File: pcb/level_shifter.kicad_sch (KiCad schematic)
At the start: 9 parts

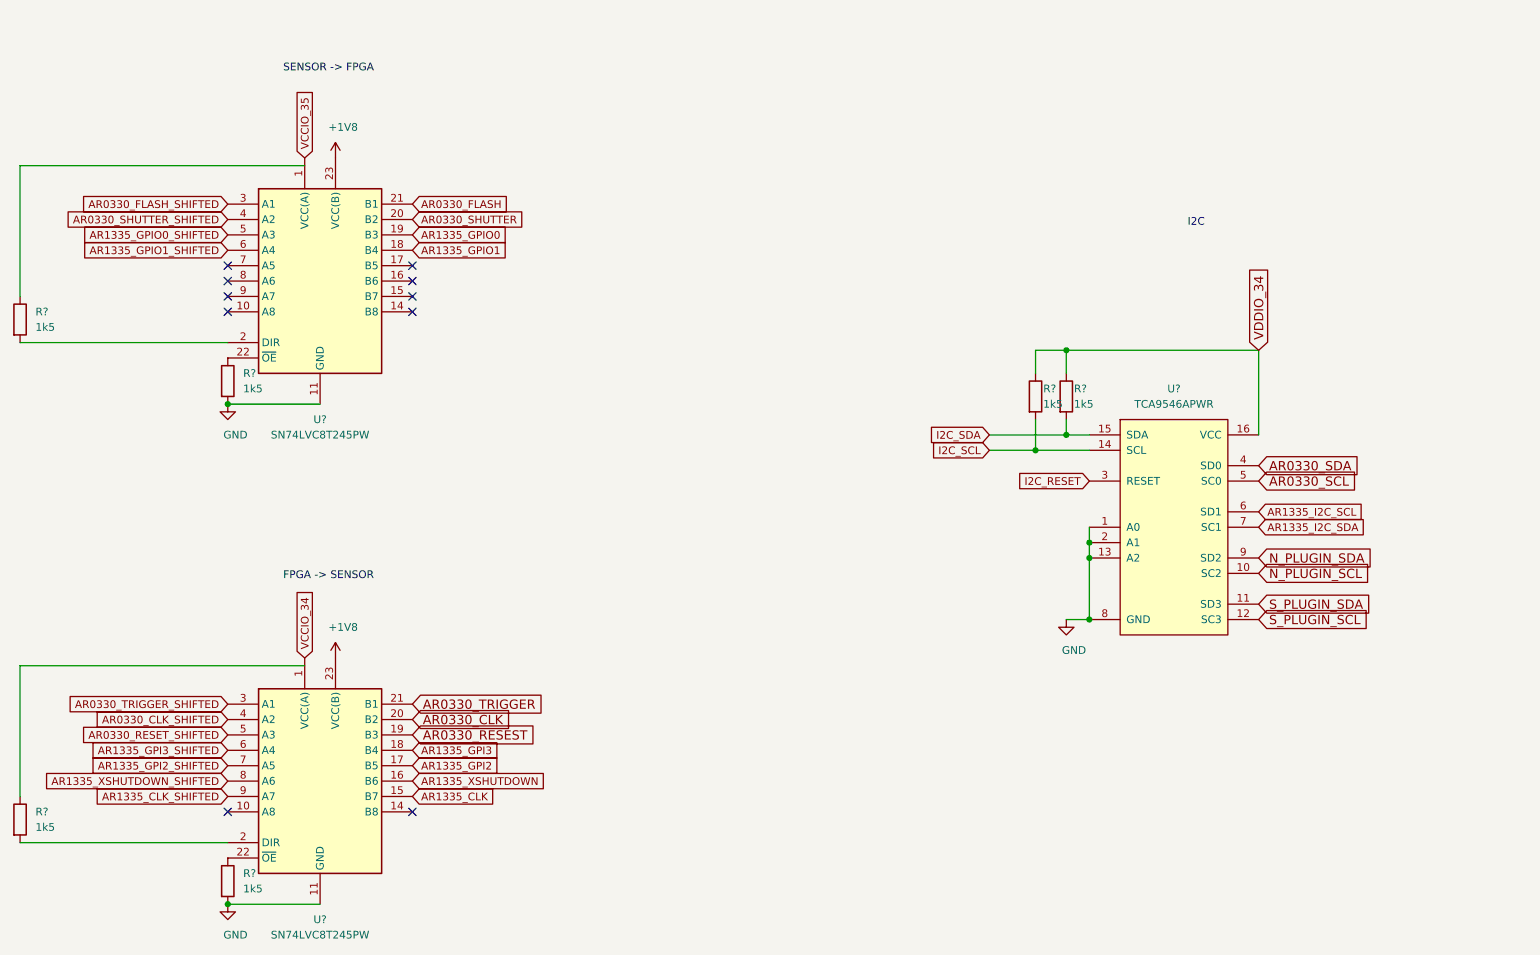
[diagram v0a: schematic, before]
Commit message: add i2c addresses
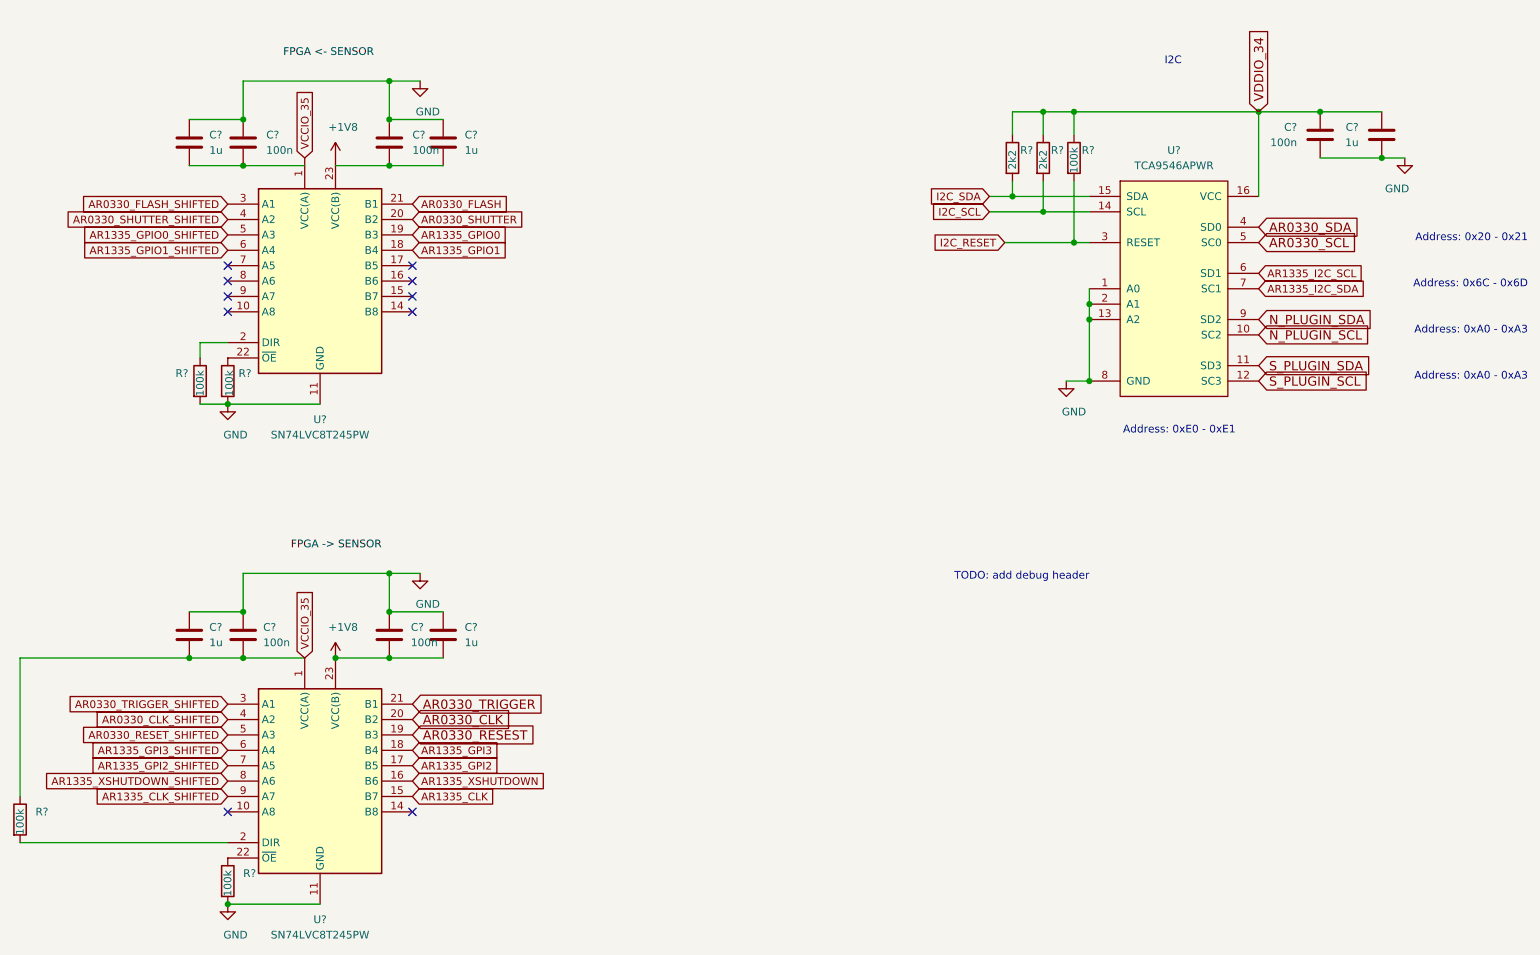
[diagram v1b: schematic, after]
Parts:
- added C? (x5): 1u, symbol Device:C
- added C? (x5): 100n, symbol Device:C
- added R?: 100k, symbol Device:R
- R? (x4): value 1k5 -> 100k
- R? (x2): value 1k5 -> 2k2
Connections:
- net VCCIO_34 is gone; now on net VCCIO_35: U?.1 (VCC(A))
- net +1V8: now also C?.2, C?.2
- net GND: now also C?.1, C?.1, C?.1, C?.1, C?.1, C?.1, C?.1, C?.1, C?.2, C?.2
- net I2C_RESET: now also R?.2
- net I2C_SCL: now also R?.2; no longer R?.2
- net I2C_SDA: now also R?.2; no longer R?.2
- net VCCIO_35: now also R?.1, C?.2, C?.2
- net VDDIO_34: now also C?.1, C?.1, R?.1
- net at R?.1: now also U?.2 (DIR)
- net at R?.2: no longer U?.2 (DIR)
- new net: C?.2, C?.2 (x2)
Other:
- note added: "Address: 0x20 - 0x21"
- note added: "Address: 0x6C - 0x6D"
- note added: "Address: 0xA0 - 0xA3"
- note added: "Address: 0xE0 - 0xE1"
- note added: "TODO: add debug header"
- moved on the sheet: R?, U?
